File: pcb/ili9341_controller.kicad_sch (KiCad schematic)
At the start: 56 parts, among them J1 USB_B_Micro, J2 RP_SWD_CONN, SW1 RP_RST_SW, SW2 RP_USB_BOOT_SW, U1 ICE40UP5K-SG48ITR, U2 LM3880, U3 LD1117S33TR_SOT223, U4 LD1117S12TR_SOT223, U5 LD1117S25TR_SOT223, U6 RP2040, U7 W25Q128JVS, Y1 12MHz

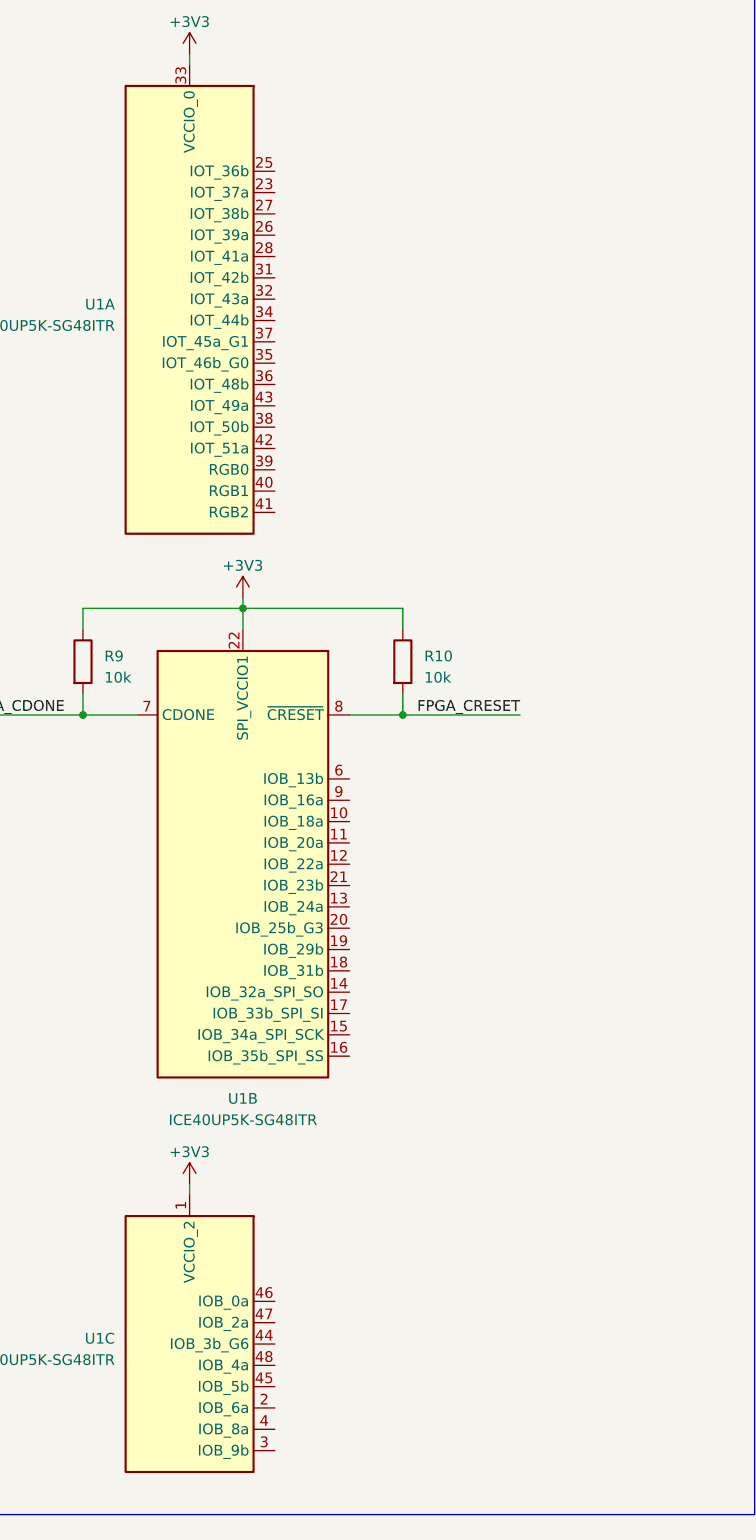
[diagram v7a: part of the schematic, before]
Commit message: assign FPGA pins in pcb, update yosys pin configuration file to reflect pcb design
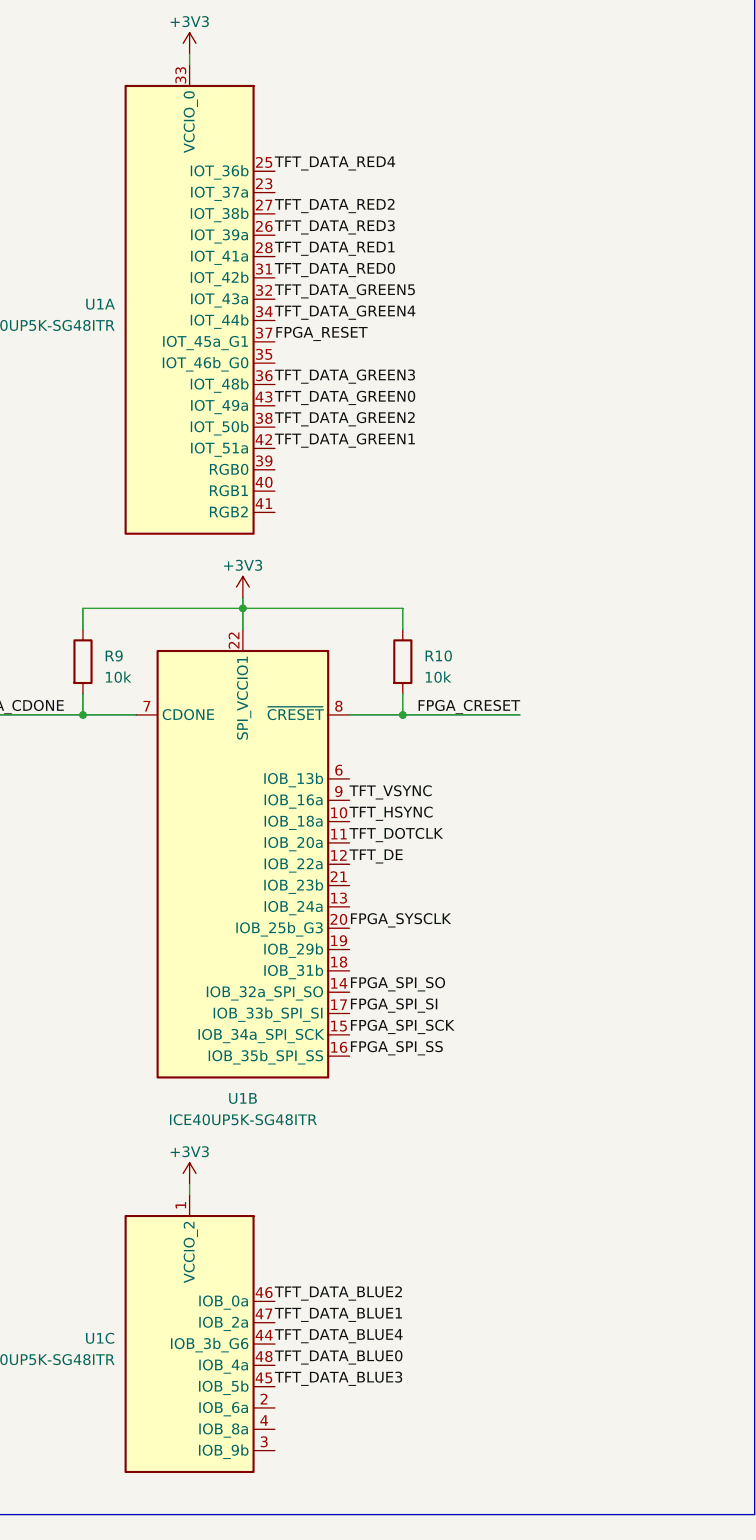
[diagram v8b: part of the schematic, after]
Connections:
- net TFT_DATA_BLUE0: now also U1.48 (IOB_4a)
- net TFT_DATA_BLUE1: now also U1.47 (IOB_2a)
- net TFT_DATA_BLUE2: now also U1.46 (IOB_0a)
- net TFT_DATA_BLUE3: now also U1.45 (IOB_5b)
- net TFT_DATA_BLUE4: now also U1.44 (IOB_3b_G6)
- net TFT_DATA_GREEN0: now also U1.43 (IOT_49a)
- net TFT_DATA_GREEN1: now also U1.42 (IOT_51a)
- net TFT_DATA_GREEN2: now also U1.38 (IOT_50b)
- net TFT_DATA_GREEN3: now also U1.36 (IOT_48b)
- net TFT_DATA_GREEN4: now also U1.34 (IOT_44b)
- net TFT_DATA_GREEN5: now also U1.32 (IOT_43a)
- net TFT_DATA_RED0: now also U1.31 (IOT_42b)
- net TFT_DATA_RED1: now also U1.28 (IOT_41a)
- net TFT_DATA_RED2: now also U1.27 (IOT_38b)
- net TFT_DATA_RED3: now also U1.26 (IOT_39a)
- net TFT_DATA_RED4: now also U1.25 (IOT_36b)
- net TFT_DE: now also U1.12 (IOB_22a)
- net TFT_DOTCLK: now also U1.11 (IOB_20a)
- net TFT_HSYNC: now also U1.10 (IOB_18a)
- net TFT_VSYNC: now also U1.9 (IOB_16a)
- net FPGA_SPI_SO: now reaches U1.14 (IOB_32a_SPI_SO)
- net FPGA_SPI_SCK: now reaches U1.15 (IOB_34a_SPI_SCK)
- net FPGA_SPI_SS: now reaches U1.16 (IOB_35b_SPI_SS)
- net FPGA_SPI_SI: now reaches U1.17 (IOB_33b_SPI_SI)
- net FPGA_SYSCLK: now reaches U1.20 (IOB_25b_G3)
- net FPGA_RESET: now reaches U1.37 (IOT_45a_G1)
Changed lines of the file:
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@@
+    (effects (font (size 1.27 1.27)) (justify left bottom))
+  )
+  (label "TFT_DATA_GREEN3" (at 262.89 83.82 0) (fields_autoplaced)
     (effects (font (size 1.27 1.27)) (justify left bottom))
   )
@@
     (effects (font (size 0.75 0.75)) (justify right bottom))
   )
+  (label "TFT_DATA_BLUE3" (at 262.89 203.2 0) (fields_autoplaced)
+    (effects (font (size 1.27 1.27)) (justify left bottom))
+  )
+  (label "TFT_DATA_RED2" (at 262.89 63.5 0) (fields_autoplaced)
+    (effects (font (size 1.27 1.27)) (justify left bottom))
+  )
+  (label "TFT_DOTCLK" (at 271.78 138.43 0) (fields_autoplaced)
+    (effects (font (size 1.27 1.27)) (justify left bottom))
+  )
   (label "TFT_DATA_RED2" (at 405.13 68.58 0) (fields_autoplaced)
     (effects (font (size 1.27 1.27)) (justify left bottom))
@@
     (effects (font (size 1.27 1.27)) (justify right bottom))
   )
+  (label "FPGA_SPI_SCK" (at 271.78 161.29 0) (fields_autoplaced)
+    (effects (font (size 1.27 1.27)) (justify left bottom))
+  )
+  (label "TFT_DATA_RED0" (at 262.89 71.12 0) (fields_autoplaced)
+    (effects (font (size 1.27 1.27)) (justify left bottom))
+  )
   (label "TFT_DATA_RED3" (at 405.13 66.04 0) (fields_autoplaced)
     (effects (font (size 1.27 1.27)) (justify left bottom))
@@
     (effects (font (size 1.27 1.27)) (justify right bottom))
   )
+  (label "TFT_DATA_GREEN0" (at 262.89 86.36 0) (fields_autoplaced)
+    (effects (font (size 1.27 1.27)) (justify left bottom))
+  )
   (label "USB_D+" (at 60.96 46.99 180) (fields_autoplaced)
     (effects (font (size 1.27 1.27)) (justify right bottom))
+  )
+  (label "TFT_DATA_BLUE1" (at 262.89 195.58 0) (fields_autoplaced)
+    (effects (font (size 1.27 1.27)) (justify left bottom))
   )
   (label "USB_D-" (at 60.96 234.95 0) (fields_autoplaced)
@@
     (effects (font (size 0.75 0.75)) (justify right bottom))
   )
+  (label "TFT_DATA_GREEN5" (at 262.89 73.66 0) (fields_autoplaced)
+    (effects (font (size 1.27 1.27)) (justify left bottom))
+  )
   (label "FPGA_CRESET" (at 292.1 123.19 180) (fields_autoplaced)
     (effects (font (size 1.27 1.27)) (justify right bottom))
@@
     (effects (font (size 1.27 1.27)) (justify right bottom))
   )
+  (label "TFT_DATA_RED4" (at 262.89 58.42 0) (fields_autoplaced)
+    (effects (font (size 1.27 1.27)) (justify left bottom))
+  )
   (label "TFT_DE" (at 364.49 80.01 180) (fields_autoplaced)
     (effects (font (size 1.27 1.27)) (justify right bottom))
@@
     (effects (font (size 1.27 1.27)) (justify right bottom))
   )
+  (label "TFT_DE" (at 271.78 140.97 0) (fields_autoplaced)
+    (effects (font (size 1.27 1.27)) (justify left bottom))
+  )
   (label "TFT_RESET" (at 364.49 57.15 180) (fields_autoplaced)
     (effects (font (size 1.27 1.27)) (justify right bottom))
+  )
+  (label "TFT_DATA_GREEN4" (at 262.89 76.2 0) (fields_autoplaced)
+    (effects (font (size 1.27 1.27)) (justify left bottom))
+  )
+  (label "FPGA_SPI_SO" (at 271.78 156.21 0) (fields_autoplaced)
+    (effects (font (size 1.27 1.27)) (justify left bottom))
+  )
+  (label "TFT_VSYNC" (at 271.78 133.35 0) (fields_autoplaced)
+    (effects (font (size 1.27 1.27)) (justify left bottom))
+  )
+  (label "TFT_DATA_GREEN1" (at 262.89 91.44 0) (fields_autoplaced)
+    (effects (font (size 1.27 1.27)) (justify left bottom))
+  )
+  (label "TFT_DATA_GREEN2" (at 262.89 88.9 0) (fields_autoplaced)
+    (effects (font (size 1.27 1.27)) (justify left bottom))
   )
   (label "TFT_CS" (at 138.43 222.25 0) (fields_autoplaced)
@@
     (effects (font (size 1.27 1.27)) (justify left bottom))
   )
+  (label "FPGA_SPI_SS" (at 271.78 163.83 0) (fields_autoplaced)
+    (effects (font (size 1.27 1.27)) (justify left bottom))
+  )
   (label "TFT_SCL" (at 138.43 227.33 0) (fields_autoplaced)
     (effects (font (size 1.27 1.27)) (justify left bottom))
@@
     (effects (font (size 1.27 1.27)) (justify left bottom))
   )
+  (label "FPGA_SYSCLK" (at 271.78 148.59 0) (fields_autoplaced)
+    (effects (font (size 1.27 1.27)) (justify left bottom))
+  )
   (label "TFT_SDI" (at 138.43 229.87 0) (fields_autoplaced)
     (effects (font (size 1.27 1.27)) (justify left bottom))
   )
+  (label "TFT_HSYNC" (at 271.78 135.89 0) (fields_autoplaced)
+    (effects (font (size 1.27 1.27)) (justify left bottom))
+  )
   (label "TFT_DATA_GREEN2" (at 405.13 86.36 0) (fields_autoplaced)
     (effects (font (size 1.27 1.27)) (justify left bottom))
   )
+  (label "TFT_DATA_BLUE4" (at 262.89 198.12 0) (fields_autoplaced)
+    (effects (font (size 1.27 1.27)) (justify left bottom))
+  )
+  (label "TFT_DATA_BLUE0" (at 262.89 200.66 0) (fields_autoplaced)
+    (effects (font (size 1.27 1.27)) (justify left bottom))
+  )
   (label "FLASH_QSPI_SD2" (at 30.48 350.52 0) (fields_autoplaced)
     (effects (font (size 1.27 1.27)) (justify left bottom))
@@
     (effects (font (size 1.27 1.27)) (justify left bottom))
   )
+  (label "FPGA_SPI_SI" (at 271.78 158.75 0) (fields_autoplaced)
+    (effects (font (size 1.27 1.27)) (justify left bottom))
+  )
   (label "TFT_DATA_GREEN1" (at 405.13 88.9 0) (fields_autoplaced)
     (effects (font (size 1.27 1.27)) (justify left bottom))
@@
     (effects (font (size 1.27 1.27)) (justify left bottom))
   )
+  (label "TFT_DATA_RED3" (at 262.89 66.04 0) (fields_autoplaced)
+    (effects (font (size 1.27 1.27)) (justify left bottom))
+  )
   (label "FLASH_QSPI_SD3" (at 30.48 353.06 0) (fields_autoplaced)
     (effects (font (size 1.27 1.27)) (justify left bottom))
@@
     (effects (font (size 1.27 1.27)) (justify left bottom))
   )
+  (label "FPGA_RESET" (at 262.89 78.74 0) (fields_autoplaced)
+    (effects (font (size 1.27 1.27)) (justify left bottom))
+  )
   (label "FLASH_QSPI_SS" (at 68.58 242.57 0) (fields_autoplaced)
     (effects (font (size 1.27 1.27)) (justify left bottom))
@@
     (effects (font (size 1.27 1.27)) (justify left bottom))
   )
+  (label "TFT_DATA_BLUE2" (at 262.89 193.04 0) (fields_autoplaced)
+    (effects (font (size 1.27 1.27)) (justify left bottom))
+  )
+  (label "TFT_DATA_RED1" (at 262.89 68.58 0) (fields_autoplaced)
+    (effects (font (size 1.27 1.27)) (justify left bottom))
+  )
